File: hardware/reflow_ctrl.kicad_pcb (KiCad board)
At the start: 2 copper layers, 22 parts, among them IC1 MAX6675, U2 MOC3063, U3 BTA41/600B, X1 Master, X2 Mains, X3 Load, X4 Thermocouple

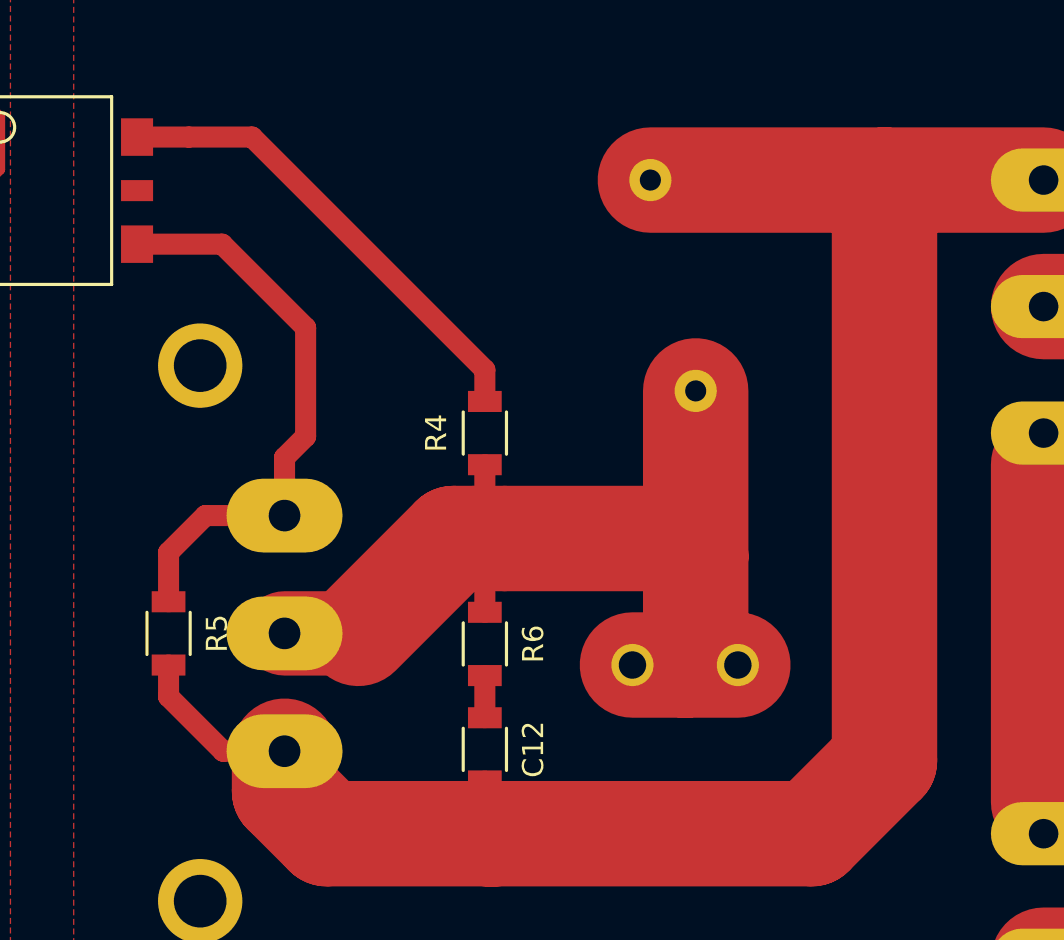
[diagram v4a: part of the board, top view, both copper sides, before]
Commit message: Use a smaller VDR package
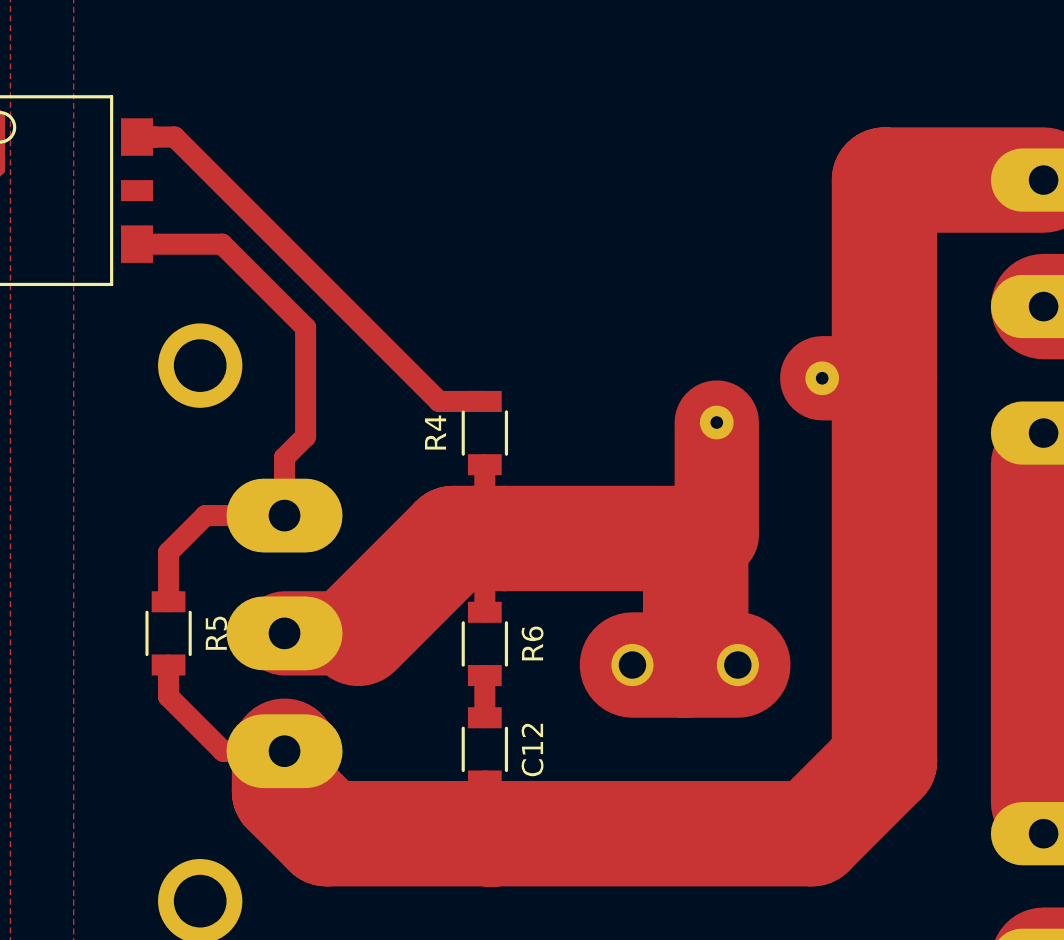
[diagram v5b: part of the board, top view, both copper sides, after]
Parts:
- VR1: footprint Varistors:RV_Disc_D21.5_W5.1_P10 -> Varistors:RV_Disc_D7_W4.5_P5
- moved VR1 1.80 mm to (174.5, 77.5), turned to 0 degrees
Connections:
- HS1 pad 1: /PE_mains -> (no net)
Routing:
- net /L_load: track 93.0 -> 84.8 mm
- net /L_main_fused: track 48.3 -> 47.0 mm
- net /MOC_A1: track 22.6 -> 21.7 mm
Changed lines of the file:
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@@
 (kicad_pcb (version 4) (host pcbnew "(2015-09-12 BZR 6188)-product")
   (general
-    (links 35)
+    (links 33)
     (no_connects 0)
-    (area 95.615476 49.075 213 132.700001)
+    (area 0 0 0 0)
     (thickness 1.6)
     (drawings 9)
-    (tracks 111)
+    (tracks 113)
     (zones 0)
     (modules 22)
@@
       (net 16 /MOC_A2))
   )
-  (module Varistors:RV_Disc_D21.5_W5.1_P10 (layer B.Cu)
-    (at 173.5 76 90)
-    (tags "varistor SIOV")
-    (fp_text reference VR1 (at 5 -4.625 90) (layer B.SilkS)
-      (effects (font (size 1 1) (thickness 0.15)) (justify mirror))
-    )
-    (fp_text value 430V (at 5 2.475 90) (layer B.Fab)
-      (effects (font (size 1 1) (thickness 0.15)) (justify mirror))
-    )
-    (fp_line (start -6 -3.875) (end 16 -3.875) (layer B.CrtYd) (width 0.05))
-    (fp_line (start -6 1.725) (end 16 1.725) (layer B.CrtYd) (width 0.05))
-    (fp_line (start 16 1.725) (end 16 -3.875) (layer B.CrtYd) (width 0.05))
-    (fp_line (start -6 1.725) (end -6 -3.875) (layer B.CrtYd) (width 0.05))
-    (fp_line (start -5.75 -3.625) (end 15.75 -3.625) (layer B.SilkS) (width 0.15))
-    (fp_line (start -5.75 1.475) (end 15.75 1.475) (layer B.SilkS) (width 0.15))
-    (fp_line (start 15.75 1.475) (end 15.75 -3.625) (layer B.SilkS) (width 0.15))
-    (fp_line (start -5.75 1.475) (end -5.75 -3.625) (layer B.SilkS) (width 0.15))
-    (pad 1 thru_hole circle (at 0 0 90) (size 2 2) (drill 1) (layers *.Cu *.Mask B.SilkS)
-      (net 17 /L_main_fused))
-    (pad 2 thru_hole circle (at 10 -2.15 90) (size 2 2) (drill 1) (layers *.Cu *.Mask B.SilkS)
-      (net 3 /L_load))
-  )
   (module uMIDI:Mains_Solder (layer B.Cu)
     (at 190 103 90)
@@
     (fp_line (start 1.6 -0.7) (end 1.6 -0.9) (layer B.SilkS) (width 0.15))
     (pad 1 thru_hole circle (at -12.7 0 90) (size 4 4) (drill 2.5) (layers *.Cu *.Mask)
-      (net 8 /PE_mains) (zone_connect 2))
+      (zone_connect 2))
     (pad 1 thru_hole circle (at 12.7 0 90) (size 4 4) (drill 2.5) (layers *.Cu *.Mask)
-      (net 8 /PE_mains) (zone_connect 2))
+      (zone_connect 2))
   )
   (module uMIDI:Semi-Optotriac_MOC3063-SMD (layer F.Cu)
@@
     (pad 4 smd trapezoid (at 2.54 -4.505 270) (size 1.78 1.52) (layers F.Cu F.Paste F.Mask)
       (net 16 /MOC_A2))
+  )
+  (module Varistors:RV_Disc_D7_W4.5_P5 (layer B.Cu)
+    (at 174.5 77.5)
+    (tags "varistor SIOV")
+    (fp_text reference VR1 (at 2.5 -4.3) (layer B.SilkS)
+      (effects (font (size 1 1) (thickness 0.15)) (justify mirror))
+    )
+    (fp_text value 430V (at 2.5 2.2) (layer B.Fab)
+      (effects (font (size 1 1) (thickness 0.15)) (justify mirror))
+    )
+    (fp_line (start -1.25 -3.55) (end 6.25 -3.55) (layer B.CrtYd) (width 0.05))
+    (fp_line (start -1.25 1.45) (end 6.25 1.45) (layer B.CrtYd) (width 0.05))
+    (fp_line (start 6.25 1.45) (end 6.25 -3.55) (layer B.CrtYd) (width 0.05))
+    (fp_line (start -1.25 1.45) (end -1.25 -3.55) (layer B.CrtYd) (width 0.05))
+    (fp_line (start -1 -3.3) (end 6 -3.3) (layer B.SilkS) (width 0.15))
+    (fp_line (start -1 1.2) (end 6 1.2) (layer B.SilkS) (width 0.15))
+    (fp_line (start 6 1.2) (end 6 -3.3) (layer B.SilkS) (width 0.15))
+    (fp_line (start -1 1.2) (end -1 -3.3) (layer B.SilkS) (width 0.15))
+    (pad 1 thru_hole circle (at 0 0) (size 1.6 1.6) (drill 0.6) (layers *.Cu *.Mask B.SilkS)
+      (net 17 /L_main_fused))
+    (pad 2 thru_hole circle (at 5 -2.1) (size 1.6 1.6) (drill 0.6) (layers *.Cu *.Mask B.SilkS)
+      (net 3 /L_load))
   )
   (gr_text "Reflow_Ctrl 0.1\n2016 by Simon Gansen" (at 175.5 122) (layer F.Cu)
@@
   (segment (start 121.905 112.7) (end 124.95 112.7) (width 0.5) (layer F.Cu) (net 2) (status 30))
   (segment (start 124.95 112.7) (end 125 112.75) (width 0.5) (layer F.Cu) (net 2) (status 30))
+  (segment (start 182.454179 93.545821) (end 182.454179 75.374221) (width 5) (layer F.Cu) (net 3))
+  (segment (start 182.454179 75.374221) (end 182.454179 66) (width 5) (layer F.Cu) (net 3))
+  (segment (start 179.5 75.4) (end 182.4284 75.4) (width 4) (layer F.Cu) (net 3))
+  (segment (start 182.4284 75.4) (end 182.454179 75.374221) (width 3) (layer F.Cu) (net 3))
   (segment (start 154 93.088) (end 151.088 93.088) (width 1) (layer F.Cu) (net 3))
   (segment (start 148.5 90.5) (end 148.5 89) (width 1) (layer F.Cu) (net 3))
@@
   (segment (start 154 95) (end 156 97) (width 5) (layer F.Cu) (net 3))
   (segment (start 179 97) (end 182.454179 93.545821) (width 5) (layer F.Cu) (net 3))
-  (segment (start 182.454179 93.545821) (end 182.454179 66) (width 5) (layer F.Cu) (net 3))
-  (segment (start 171.35 66) (end 182.454179 66) (width 5) (layer F.Cu) (net 3))
   (segment (start 154 93.088) (end 154.412 93.5) (width 3) (layer F.Cu) (net 3) (status 30))
   (segment (start 190 109) (end 171.5 109) (width 5) (layer F.Cu) (net 4))
@@
   (segment (start 111.27 84.96) (end 111.24 84.96) (width 0.3) (layer F.Cu) (net 13) (status 30))
   (segment (start 163.5 89.5) (end 163.5 91.5) (width 1) (layer F.Cu) (net 14) (status 30))
-  (segment (start 163.5 76.5) (end 163.5 75) (width 1) (layer F.Cu) (net 15))
-  (segment (start 163.5 75) (end 152.46 63.96) (width 1) (layer F.Cu) (net 15))
-  (segment (start 152.46 63.96) (end 149.46 63.96) (width 1) (layer F.Cu) (net 15))
-  (segment (start 147.005 63.96) (end 149.46 63.96) (width 1) (layer F.Cu) (net 15))
+  (segment (start 163.5 76.5) (end 161.328441 76.5) (width 1) (layer F.Cu) (net 15))
+  (segment (start 161.328441 76.5) (end 148.788441 63.96) (width 1) (layer F.Cu) (net 15))
+  (segment (start 148.788441 63.96) (end 147.865 63.96) (width 1) (layer F.Cu) (net 15))
+  (segment (start 147.865 63.96) (end 147.005 63.96) (width 1) (layer F.Cu) (net 15))
   (segment (start 155 73) (end 151.04 69.04) (width 1) (layer F.Cu) (net 16))
   (segment (start 151.04 69.04) (end 147.005 69.04) (width 1) (layer F.Cu) (net 16))
@@
   (segment (start 148.5 83.66118) (end 150.24918 81.912) (width 1) (layer F.Cu) (net 16))
   (segment (start 150.24918 81.912) (end 154 81.912) (width 1) (layer F.Cu) (net 16))
+  (segment (start 173.5 83.849853) (end 174.5 82.849853) (width 3) (layer F.Cu) (net 17))
+  (segment (start 174.5 82.849853) (end 174.5 77.5) (width 4) (layer F.Cu) (net 17))
   (segment (start 163.5 79.5) (end 163.5 81.5) (width 1) (layer F.Cu) (net 17))
   (segment (start 163.5 81.5) (end 162 83) (width 1) (layer F.Cu) (net 17))
@@
   (segment (start 157.5 87.5) (end 162 83) (width 5) (layer F.Cu) (net 17))
   (segment (start 154 87.5) (end 157.5 87.5) (width 4) (layer F.Cu) (net 17))
-  (segment (start 173.5 76) (end 173.5 83.849853) (width 5) (layer F.Cu) (net 17))
   (segment (start 173.5 83.849853) (end 173.5 88.505825) (width 5) (layer F.Cu) (net 17))
-  (segment (start 173.349853 84) (end 173.5 83.849853) (width 3) (layer F.Cu) (net 17))
   (segment (start 175.5 89) (end 173.005825 89) (width 5) (layer F.Cu) (net 17))
   (segment (start 173.005825 89) (end 170.5 89) (width 5) (layer F.Cu) (net 17))
